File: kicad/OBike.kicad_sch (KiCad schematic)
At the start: 69 parts, among them J1 F34G-1A7Q1-E8C40, J2 Micro_SD_Card_Det1, J3 Conn_01x02, J4 Conn_01x04, J5 U.FL-R-SMT-1_10_, J7 Conn_01x05, Q1 SS8050, SW1 5_position_tactile, U1 DPS368XTSA1, U10 MAX40200AUK, U2 DS3231M, U3 MCP23017_SO, U4 74HC14, U5 Seeed Studio XIAO SAMD21, U6 MAX40200AUK, U7 LC76G, U8 MAX40200AUK, U9 W25N01GVZEIG_TR

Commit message: buzzer
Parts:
- added J6: Conn_01x02, Connector_PinHeader_2.00mm:PinHeader_1x02_P2.00mm_Vertical, symbol Connector_Generic:Conn_01x02
- added Q2: SS8050, Package_TO_SOT_SMD:SOT-23, symbol Transistor_BJT:SS8050
- added R15: 1K, Resistor_SMD:R_0603_1608Metric, symbol Device:R
- added R18: 10K, Resistor_SMD:R_0603_1608Metric, symbol Device:R
- LS1: value PK-11N40PQ -> ASI09N40MTRQ; footprint Mallory:PK-11N40PQ_MAL -> Mallory:ASI09N40M
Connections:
- net AUX_3V3: now also LS1.1
- net BAT+: now also J6.2 (Pin_2)
- net BAT-: now also J6.1 (Pin_1)
- net BUZZ: now also R15.1; no longer LS1.1
- net GND: now also Q2.2 (E), R18.1; no longer LS1.2
- new net: LS1.2, Q2.3 (C)
- new net: Q2.1 (B), R15.2, R18.2
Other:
- moved on the sheet: LS1

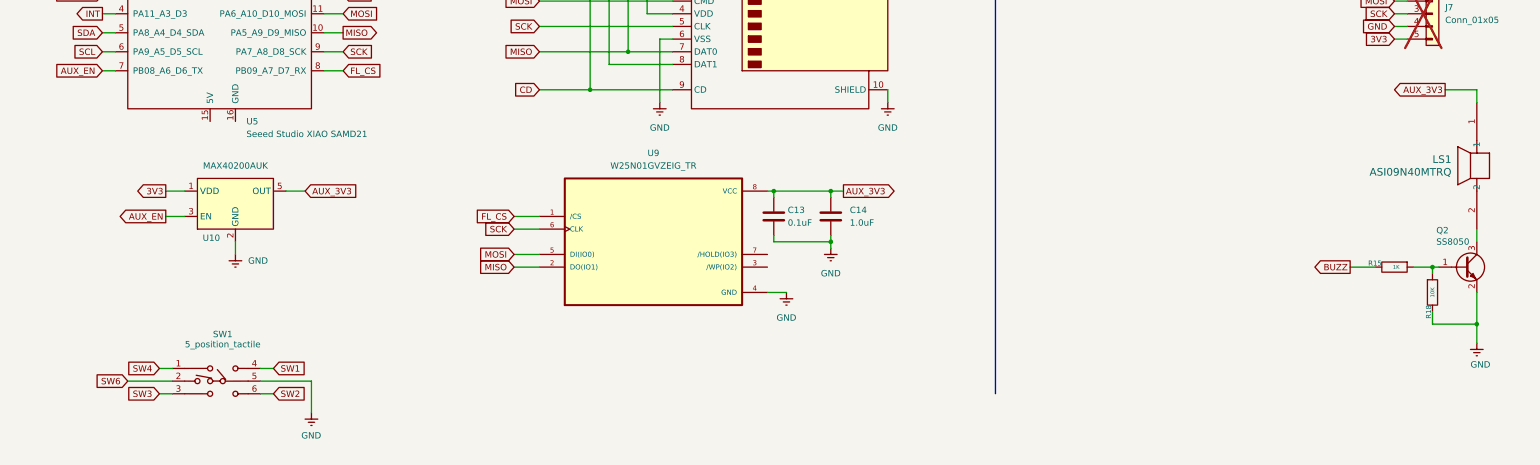
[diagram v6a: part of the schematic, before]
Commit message: PCB speaker
- buzzer now uses a header rather than SMD
- added buzzer code to HAL
- small fixes to tcx logger
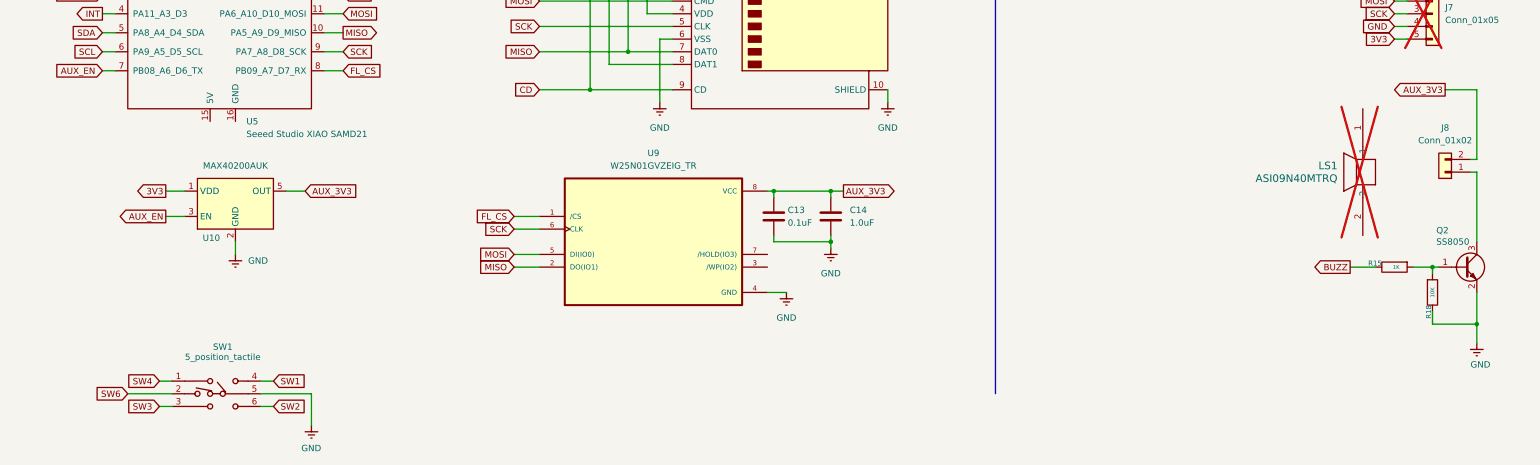
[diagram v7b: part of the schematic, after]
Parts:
- added J8: Conn_01x02, Connector_PinHeader_2.00mm:PinHeader_1x02_P2.00mm_Vertical, symbol Connector_Generic:Conn_01x02
- LS1: now not fitted
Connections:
- net AUX_3V3: now also J8.2 (Pin_2); no longer LS1.1
- net at Q2.3 (C): now also J8.1 (Pin_1); no longer LS1.2
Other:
- moved on the sheet: SW1
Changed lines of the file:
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@@
 	(wire
 		(pts
-			(xy 152.4 248.92) (xy 154.94 248.92)
+			(xy 152.4 251.46) (xy 154.94 251.46)
 		)
 		(stroke
@@
 	(wire
 		(pts
-			(xy 152.4 254) (xy 154.94 254)
+			(xy 152.4 256.54) (xy 154.94 256.54)
 		)
 		(stroke
@@
 	(wire
 		(pts
-			(xy 132.08 254) (xy 134.62 254)
+			(xy 132.08 256.54) (xy 134.62 256.54)
 		)
 		(stroke
@@
 	(wire
 		(pts
-			(xy 396.24 220.98) (xy 396.24 223.52)
-		)
-		(stroke
-			(width 0)
-			(type default)
-		)
-	)
-	(wire
-		(pts
 			(xy 157.48 213.36) (xy 161.29 213.36)
 		)
@@
 	(wire
 		(pts
-			(xy 132.08 248.92) (xy 134.62 248.92)
+			(xy 132.08 251.46) (xy 134.62 251.46)
 		)
 		(stroke
@@
 	(wire
 		(pts
+			(xy 396.24 193.04) (xy 396.24 207.01)
+		)
+		(stroke
+			(width 0)
+			(type default)
+		)
+	)
+	(wire
+		(pts
 			(xy 223.52 113.03) (xy 224.79 113.03)
 		)
@@
 	(wire
 		(pts
-			(xy 162.56 251.46) (xy 162.56 257.81)
+			(xy 162.56 254) (xy 162.56 260.35)
 		)
 		(stroke
@@
 	(wire
 		(pts
-			(xy 152.4 251.46) (xy 162.56 251.46)
+			(xy 152.4 254) (xy 162.56 254)
 		)
 		(stroke
@@
 	(wire
 		(pts
-			(xy 389.89 193.04) (xy 396.24 193.04)
+			(xy 396.24 193.04) (xy 389.89 193.04)
 		)
 		(stroke
@@
 	(wire
 		(pts
+			(xy 396.24 207.01) (xy 394.97 207.01)
+		)
+		(stroke
+			(width 0)
+			(type default)
+		)
+	)
+	(wire
+		(pts
 			(xy 368.3 39.37) (xy 382.27 39.37)
 		)
@@
 	(wire
 		(pts
-			(xy 125.73 251.46) (xy 134.62 251.46)
+			(xy 125.73 254) (xy 134.62 254)
 		)
 		(stroke
@@
 	(wire
 		(pts
+			(xy 396.24 209.55) (xy 394.97 209.55)
+		)
+		(stroke
+			(width 0)
+			(type default)
+		)
+	)
+	(wire
+		(pts
 			(xy 330.2 118.11) (xy 334.01 118.11)
 		)
@@
 	(wire
 		(pts
+			(xy 396.24 223.52) (xy 396.24 209.55)
+		)
+		(stroke
+			(width 0)
+			(type default)
+		)
+	)
+	(wire
+		(pts
 			(xy 30.48 105.41) (xy 34.29 105.41)
 		)
@@
 	(wire
 		(pts
-			(xy 396.24 193.04) (xy 396.24 195.58)
-		)
-		(stroke
-			(width 0)
-			(type default)
-		)
-	)
-	(wire
-		(pts
 			(xy 161.29 36.83) (xy 161.29 39.37)
 		)
@@
 	(global_label "SW6"
 		(shape input)
-		(at 125.73 251.46 180)
+		(at 125.73 254 180)
 		(fields_autoplaced yes)
 		(effects
@@
 		)
 		(property "Intersheetrefs" "${INTERSHEET_REFS}"
-			(at 118.8744 251.46 0)
+			(at 118.8744 254 0)
 			(effects
 				(font
@@
 	(global_label "SW4"
 		(shape input)
-		(at 132.08 248.92 180)
+		(at 132.08 251.46 180)
 		(fields_autoplaced yes)
 		(effects
@@
 		)
 		(property "Intersheetrefs" "${INTERSHEET_REFS}"
-			(at 125.2244 248.92 0)
+			(at 125.2244 251.46 0)
 			(effects
 				(font
@@
 	(global_label "SW1"
 		(shape input)
-		(at 154.94 248.92 0)
+		(at 154.94 251.46 0)
 		(fields_autoplaced yes)
 		(effects
@@
 		)
 		(property "Intersheetrefs" "${INTERSHEET_REFS}"
-			(at 161.7956 248.92 0)
+			(at 161.7956 251.46 0)
 			(effects
 				(font
@@
 	(global_label "SW2"
 		(shape input)
-		(at 154.94 254 0)
+		(at 154.94 256.54 0)
 		(fields_autoplaced yes)
 		(effects
@@
 		)
 		(property "Intersheetrefs" "${INTERSHEET_REFS}"
-			(at 161.7956 254 0)
+			(at 161.7956 256.54 0)
 			(effects
 				(font
@@
 	(global_label "SW3"
 		(shape input)
-		(at 132.08 254 180)
+		(at 132.08 256.54 180)
 		(fields_autoplaced yes)
 		(effects
@@
 		)
 		(property "Intersheetrefs" "${INTERSHEET_REFS}"
-			(at 125.2244 254 0)
+			(at 125.2244 256.54 0)
 			(effects
 				(font
@@
 	(symbol
 		(lib_id "power:Earth")
-		(at 162.56 257.81 0)
+		(at 162.56 260.35 0)
 		(unit 1)
 		(exclude_from_sim no)
@@
 		(dnp no)
 		(property "Reference" "#PWR07"
-			(at 162.56 264.16 0)
+			(at 162.56 266.7 0)
 			(effects
 				(font
@@
 		)
 		(property "Value" "GND"
-			(at 160.528 262.382 0)
+			(at 160.528 264.922 0)
 			(effects
 				(font
@@
 		)
 		(property "Footprint" ""
-			(at 162.56 257.81 0)
+			(at 162.56 260.35 0)
 			(effects
 				(font
@@
 		)
 		(property "Datasheet" "~"
-			(at 162.56 257.81 0)
+			(at 162.56 260.35 0)
 			(effects
 				(font
@@
 		)
 		(property "Description" "Power symbol creates a global label with name \"Earth\""
-			(at 162.56 257.81 0)
+			(at 162.56 260.35 0)
 			(effects
 				(font
@@
 		(lib_name "5_position_tactile_1")
 		(lib_id "5_pos:5_position_tactile")
-		(at 144.78 251.46 0)
+		(at 144.78 254 0)
 		(unit 1)
 		(exclude_from_sim no)
@@
 		(dnp no)
 		(property "Reference" "SW1"
-			(at 144.78 242.062 0)
+			(at 144.78 244.602 0)
 			(effects
 				(font
@@
 		)
 		(property "Value" "5_position_tactile"
-			(at 144.78 244.094 0)
+			(at 144.78 246.634 0)
 			(effects
 				(font
@@
 		)
 		(property "Footprint" "5_pos:5-position"
-			(at 144.78 251.46 0)
+			(at 144.78 254 0)
 			(effects
 				(font
@@
 		)
 		(property "Datasheet" "~"
-			(at 144.78 251.46 0)
+			(at 144.78 254 0)
 			(effects
 				(font
@@
 		)
 		(property "Description" "Single Pole Single Throw (SPST) switch"
-			(at 144.78 243.84 0)
+			(at 144.78 246.38 0)
 			(effects
 				(font
@@
 		)
 		(property "Manufacturer" "TE Connectivity ALCOSWITCH Switches"
-			(at 144.78 251.46 0)
+			(at 144.78 254 0)
 			(effects
 				(font
@@
 		)
 		(property "Manufacturer PN" "2425755-1"
-			(at 144.78 251.46 0)
+			(at 144.78 254 0)
 			(effects
 				(font
@@
 		)
 		(property "Digikiey PN" "450-2425755-1CT-ND"
-			(at 144.78 251.46 0)
+			(at 144.78 254 0)
 			(effects
 				(font
@@
 		)
 		(property "MANUFACTURER" ""
-			(at 144.78 251.46 0)
+			(at 144.78 254 0)
 			(effects
 				(font
@@
 		)
 		(property "Field6" ""
-			(at 144.78 251.46 0)
+			(at 144.78 254 0)
 			(effects
 				(font
@@
 	)
 	(symbol
+		(lib_id "Connector_Generic:Conn_01x02")
+		(at 389.89 209.55 180)
+		(unit 1)
+		(exclude_from_sim no)
+		(in_bom yes)
+		(on_board yes)
+		(dnp no)
+		(fields_autoplaced yes)
+		(property "Reference" "J8"
+			(at 389.89 200.66 0)
+			(effects
+				(font
+					(size 1.27 1.27)
+				)
+			)
+		)
+		(property "Value" "Conn_01x02"
+			(at 389.89 203.2 0)
+			(effects
+				(font
+					(size 1.27 1.27)
+				)
+			)
+		)
+		(property "Footprint" "Connector_PinHeader_2.00mm:PinHeader_1x02_P2.00mm_Vertical"
+			(at 389.89 209.55 0)
+			(effects
+				(font
+					(size 1.27 1.27)
+				)
+				(hide yes)
+			)
+		)
+		(property "Datasheet" "~"
+			(at 389.89 209.55 0)
+			(effects
+				(font
+					(size 1.27 1.27)
+				)
+				(hide yes)
+			)
+		)
+		(property "Description" "Generic connector, single row, 01x02, script generated (kicad-library-utils/schlib/autogen/connector/)"
+			(at 389.89 209.55 0)
+			(effects
+				(font
+					(size 1.27 1.27)
+				)
+				(hide yes)
+			)
+		)
+		(pin "1"
+		)
+		(pin "2"
+		)
+		(instances
+			(project "OBike"
+				(path "/b6c91502-91b9-44d0-9569-7774925b5f71"
+					(reference "J8")
+					(unit 1)
+				)
+			)
+		)
+	)
+	(symbol
 		(lib_id "Device:C")
 		(at 207.01 44.45 0)
@@
 	(symbol
 		(lib_id "Mallory:PK-11N40PQ")
-		(at 396.24 195.58 90)
+		(at 373.38 196.85 90)
 		(mirror x)
 		(unit 1)
@@
 		(in_bom yes)
 		(on_board yes)
-		(dnp no)
+		(dnp yes)
 		(property "Reference" "LS1"
-			(at 391.16 207.0099 90)
+			(at 368.3 208.2799 90)
 			(effects
 				(font
@@
 		)
 		(property "Value" "ASI09N40MTRQ"
-			(at 391.16 209.5499 90)
+			(at 368.3 210.8199 90)
 			(effects
 				(font
@@
 		)
 		(property "Footprint" "Mallory:ASI09N40M"
-			(at 396.24 195.58 0)
+			(at 373.38 196.85 0)
 			(effects
 				(font
@@
 		)
 		(property "Datasheet" "PK-11N40PQ"
-			(at 396.24 195.58 0)
+			(at 373.38 196.85 0)
 			(effects
 				(font
@@
 		)
 		(property "Description" ""
-			(at 396.24 195.58 0)
+			(at 373.38 196.85 0)
 			(effects
 				(font

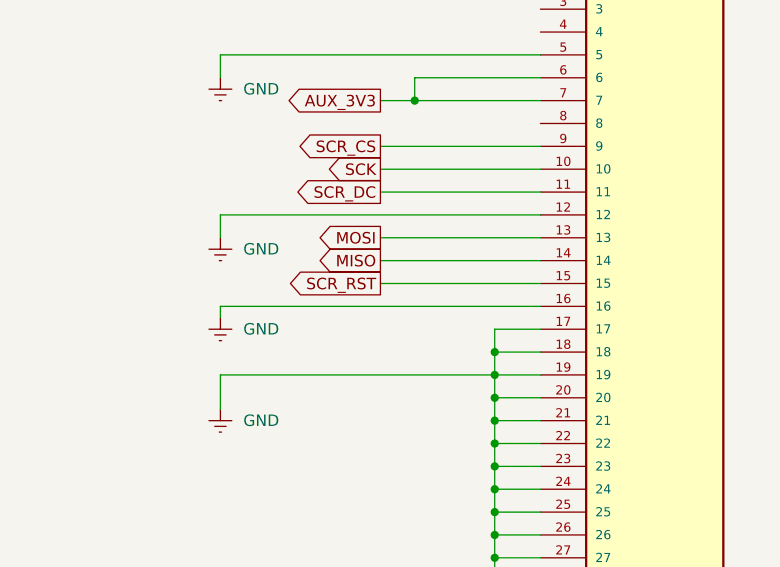
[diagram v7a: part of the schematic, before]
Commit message: schem updates
- added locating holes for screen to PCB
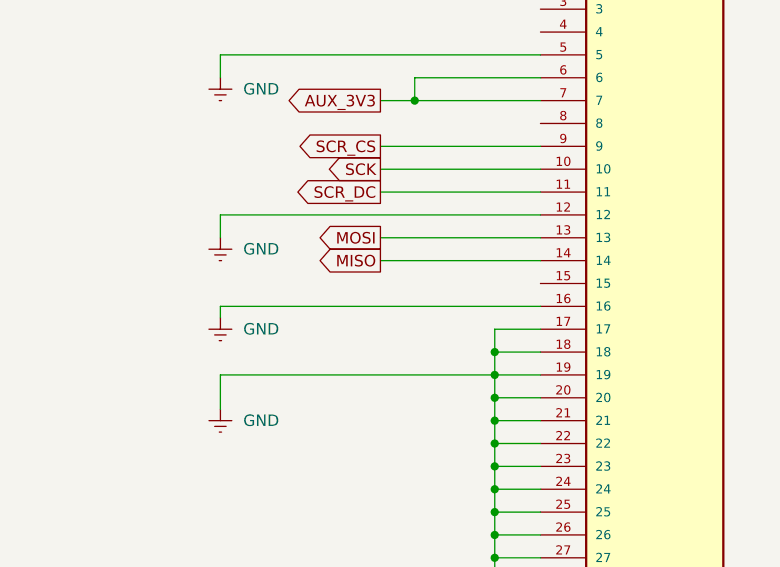
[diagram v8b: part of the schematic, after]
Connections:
- net SCR_RST: no longer names the net of J1.15
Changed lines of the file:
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@@
 	(wire
 		(pts
-			(xy 364.49 59.69) (xy 382.27 59.69)
-		)
-		(stroke
-			(width 0)
-			(type default)
-		)
-	)
-	(wire
-		(pts
 			(xy 377.19 67.31) (xy 382.27 67.31)
 		)
@@
 			(effects
 				(font
-					(size 1.27 1.27)
-				)
-				(justify right)
-				(hide yes)
-			)
-		)
-	)
-	(global_label "SCR_RST"
-		(shape output)
-		(at 364.49 59.69 180)
-		(fields_autoplaced yes)
-		(effects
-			(font
-				(size 1.27 1.27)
-			)
-			(justify right)
-		)
-		(property "Intersheetrefs" "${INTERSHEET_REFS}"
-			(at 353.3406 59.69 0)
-			(effects
-				(font
